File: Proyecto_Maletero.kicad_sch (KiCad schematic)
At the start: 1 part

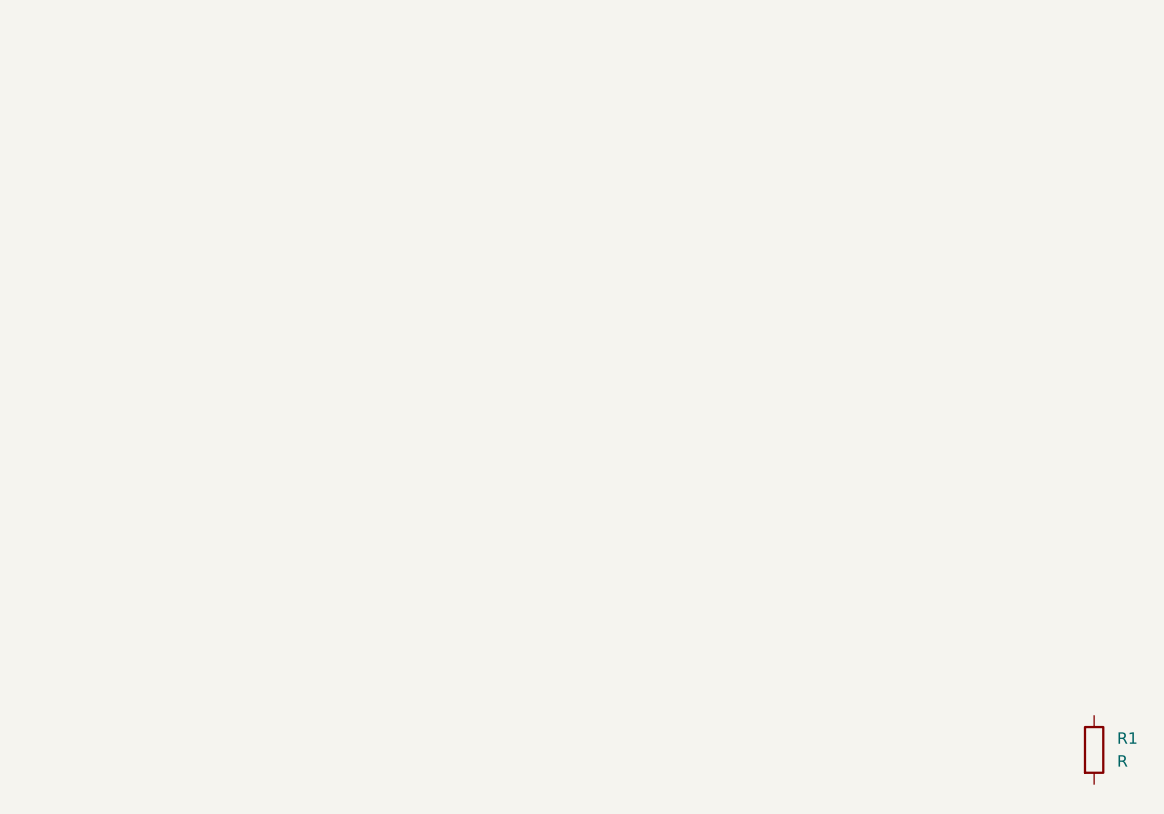
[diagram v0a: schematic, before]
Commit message: Adición conectores
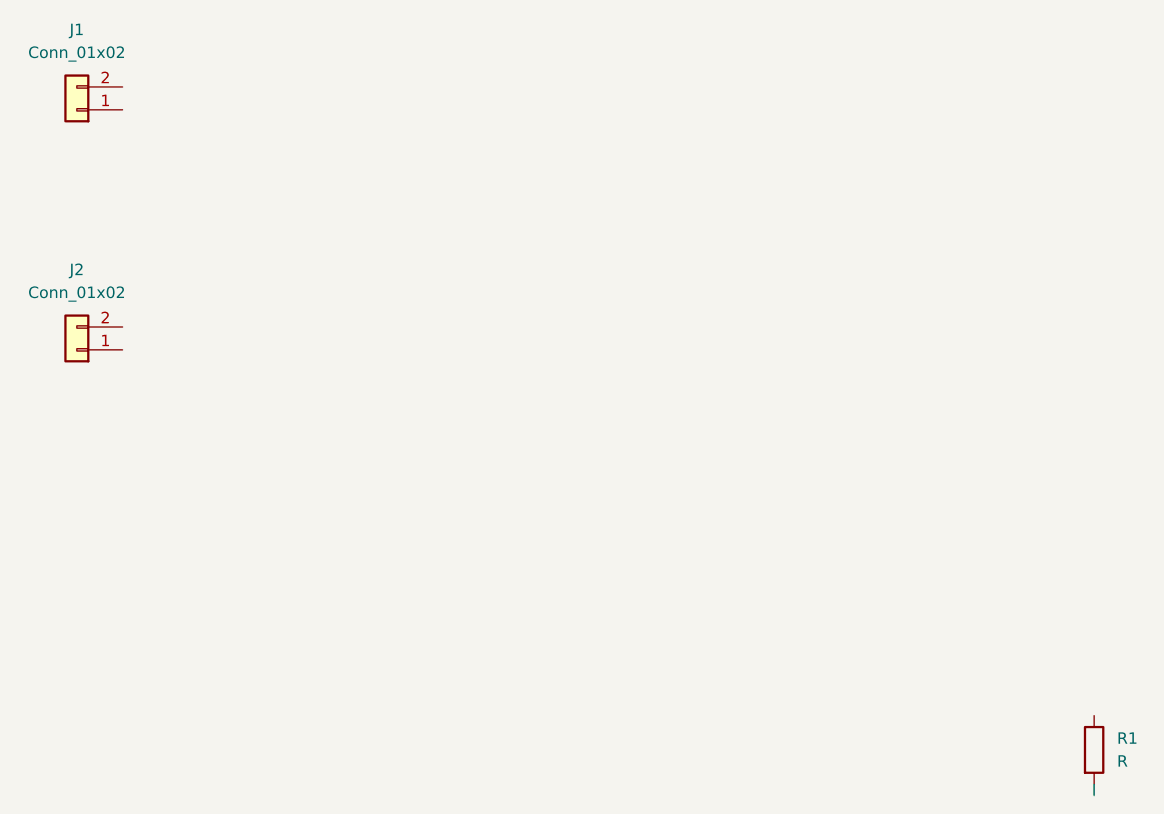
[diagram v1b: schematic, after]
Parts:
- added J1, J2: Conn_01x02, symbol Connector_Generic:Conn_01x02
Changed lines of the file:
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@@
 	(generator_version "9.0")
 	(paper "A4")
+	(wire
+		(pts
+			(xy 140.97 105.41) (xy 140.97 106.68)
+		)
+		(stroke
+			(width 0)
+			(type default)
+		)
+	)
+	(symbol
+		(lib_id "Connector_Generic:Conn_01x02")
+		(at 27.94 30.48 180)
+		(unit 1)
+		(exclude_from_sim no)
+		(in_bom yes)
+		(on_board yes)
+		(dnp no)
+		(fields_autoplaced yes)
+		(property "Reference" "J1"
+			(at 27.94 21.59 0)
+			(effects
+				(font
+					(size 1.27 1.27)
+				)
+			)
+		)
+		(property "Value" "Conn_01x02"
+			(at 27.94 24.13 0)
+			(effects
+				(font
+					(size 1.27 1.27)
+				)
+			)
+		)
+		(property "Footprint" ""
+			(at 27.94 30.48 0)
+			(effects
+				(font
+					(size 1.27 1.27)
+				)
+				(hide yes)
+			)
+		)
+		(property "Datasheet" "~"
+			(at 27.94 30.48 0)
+			(effects
+				(font
+					(size 1.27 1.27)
+				)
+				(hide yes)
+			)
+		)
+		(property "Description" "Generic connector, single row, 01x02, script generated (kicad-library-utils/schlib/autogen/connector/)"
+			(at 27.94 30.48 0)
+			(effects
+				(font
+					(size 1.27 1.27)
+				)
+				(hide yes)
+			)
+		)
+		(pin "2"
+		)
+		(pin "1"
+		)
+		(instances
+			(project ""
+				(path "/14c0d961-a62d-4b1a-b8ec-37f60ffee5fd"
+					(reference "J1")
+					(unit 1)
+				)
+			)
+		)
+	)
+	(symbol
+		(lib_id "Connector_Generic:Conn_01x02")
+		(at 27.94 57.15 180)
+		(unit 1)
+		(exclude_from_sim no)
+		(in_bom yes)
+		(on_board yes)
+		(dnp no)
+		(fields_autoplaced yes)
+		(property "Reference" "J2"
+			(at 27.94 48.26 0)
+			(effects
+				(font
+					(size 1.27 1.27)
+				)
+			)
+		)
+		(property "Value" "Conn_01x02"
+			(at 27.94 50.8 0)
+			(effects
+				(font
+					(size 1.27 1.27)
+				)
+			)
+		)
+		(property "Footprint" ""
+			(at 27.94 57.15 0)
+			(effects
+				(font
+					(size 1.27 1.27)
+				)
+				(hide yes)
+			)
+		)
+		(property "Datasheet" "~"
+			(at 27.94 57.15 0)
+			(effects
+				(font
+					(size 1.27 1.27)
+				)
+				(hide yes)
+			)
+		)
+		(property "Description" "Generic connector, single row, 01x02, script generated (kicad-library-utils/schlib/autogen/connector/)"
+			(at 27.94 57.15 0)
+			(effects
+				(font
+					(size 1.27 1.27)
+				)
+				(hide yes)
+			)
+		)
+		(pin "2"
+		)
+		(pin "1"
+		)
+		(instances
+			(project "Proyecto_Maletero"
+				(path "/14c0d961-a62d-4b1a-b8ec-37f60ffee5fd"
+					(reference "J2")
+					(unit 1)
+				)
+			)
+		)
+	)
 	(symbol
 		(lib_id "Device:R")

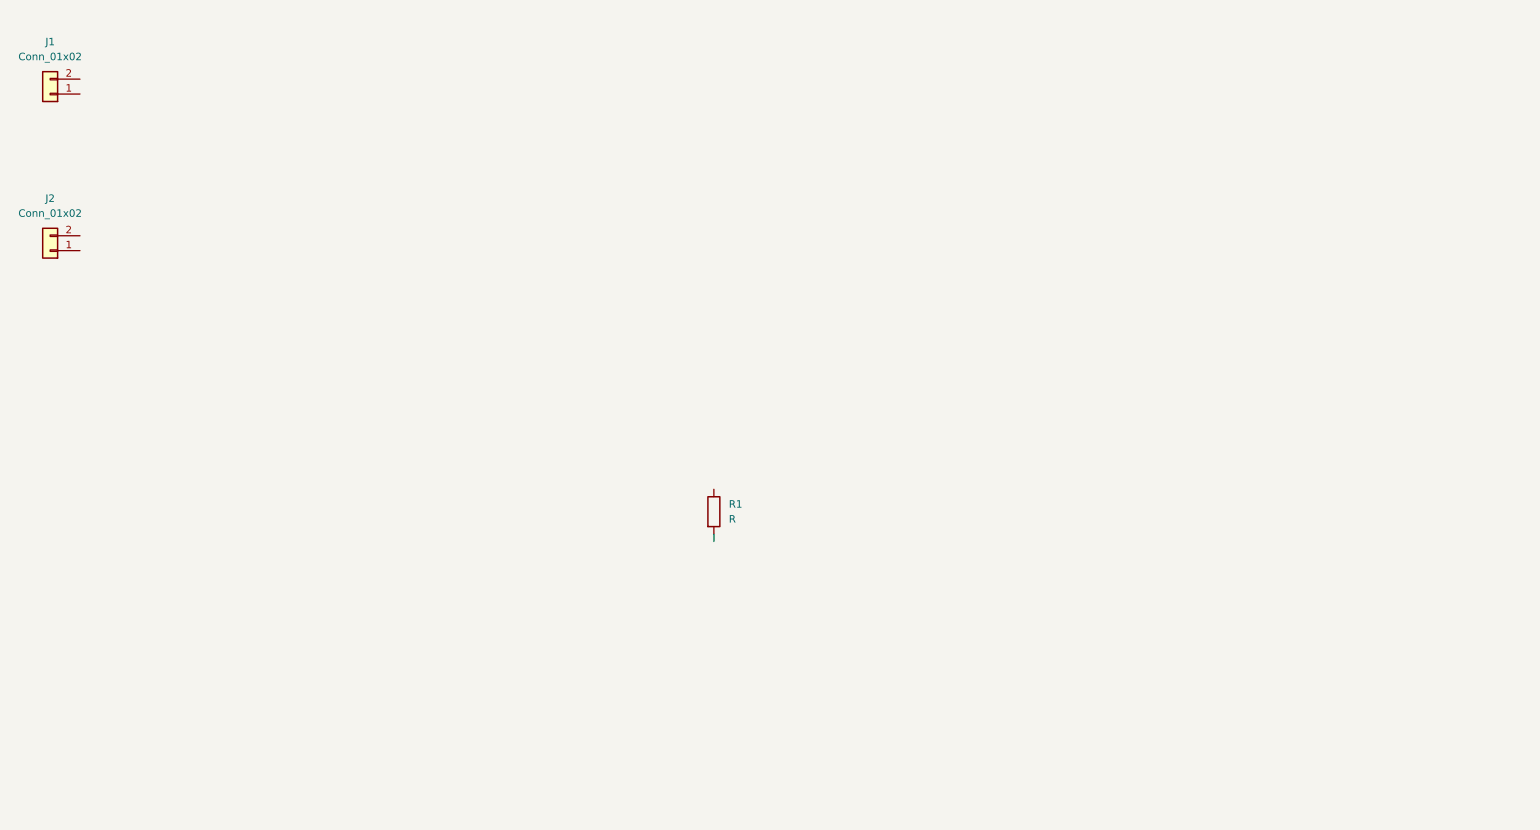
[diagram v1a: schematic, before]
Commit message: Etapa de regulacion (LT1117)
Hemos añadido una etapa de regulación  de VBAT.
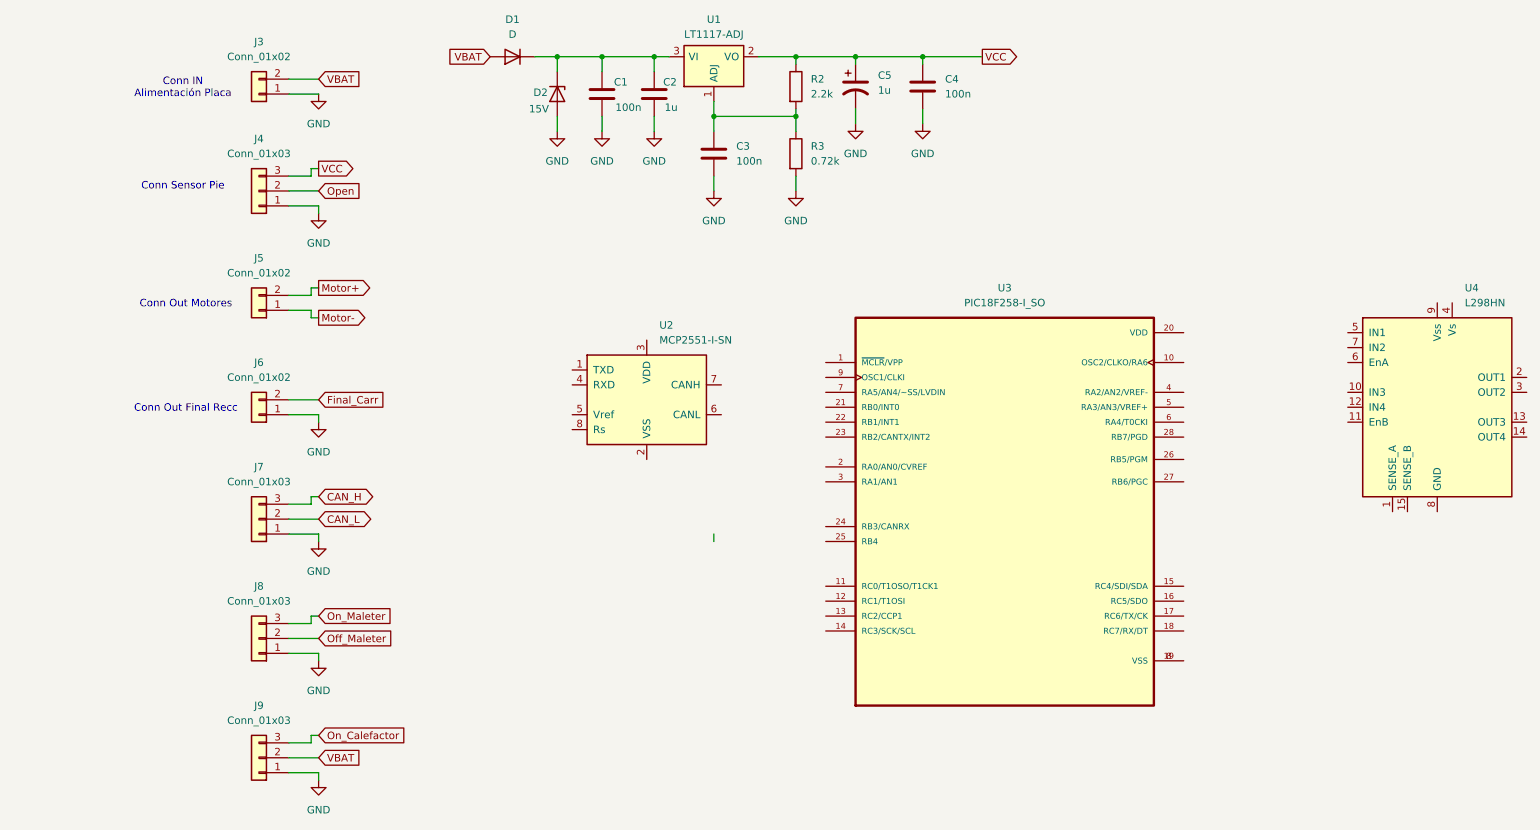
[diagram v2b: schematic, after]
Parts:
- removed J1, J2: Conn_01x02, symbol Connector_Generic:Conn_01x02
- removed R1: R, symbol Device:R
- added C1, C3, C4: 100n, symbol Device:C
- added C2: 1u, symbol Device:C
- added C5: 1u, symbol Device:C_Polarized_US
- added D1: D, symbol Device:D
- added D2: 15V, symbol Device:D_Zener
- added J3, J5, J6: Conn_01x02, TerminalBlock_Phoenix:TerminalBlock_Phoenix_MKDS-1,5-2-5.08_1x02_P5.08mm_Horizontal, symbol Connector_Generic:Conn_01x02
- added J4, J7, J8, J9: Conn_01x03, symbol Connector_Generic:Conn_01x03
- added R2: 2.2k, symbol Device:R
- added R3: 0.72k, symbol Device:R
- added U1: LT1117-ADJ, symbol Regulator_Linear:LT1117-ADJ
- added U2: MCP2551-I-SN, Package_SO:SOIC-8_3.9x4.9mm_P1.27mm, symbol Interface_CAN_LIN:MCP2551-I-SN
- added U3: PIC18F258-I_SO, PIC18F258-I_SO:SOIC127P1030X265-28N, symbol PIC18F258-I_SO:PIC18F258-I_SO
- added U4: L298HN, Package_TO_SOT_THT:TO-220-15_P2.54x2.54mm_StaggerOdd_Lead5.84mm_TabDown, symbol Driver_Motor:L298HN
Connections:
- new net: C3.1, R2.2, R3.1, U1.1 (ADJ)
- new net: C1.1, C2.1, D1.1 (K), D2.1 (K), U1.3 (VI)
- new net: U3.19 (VSS), U3.8 (VSS)
- new net CAN_H: J7.3 (Pin_3)
- new net CAN_L: J7.2 (Pin_2)
- new net Final_Carr: J6.2 (Pin_2)
- new net GND: C1.2, C2.2, C3.2, C4.2, C5.2, D2.2 (A), J3.1 (Pin_1), J4.1 (Pin_1), J6.1 (Pin_1), J7.1 (Pin_1), J8.1 (Pin_1), J9.1 (Pin_1), R3.2
- new net Motor+: J5.2 (Pin_2)
- new net Motor-: J5.1 (Pin_1)
- new net Off_Maleter: J8.2 (Pin_2)
- new net On_Calefactor: J9.3 (Pin_3)
- new net On_Maleter: J8.3 (Pin_3)
- new net Open: J4.2 (Pin_2)
- new net VBAT: D1.2 (A), J3.2 (Pin_2), J9.2 (Pin_2)
- new net VCC: C4.1, C5.1, J4.3 (Pin_3), R2.1, U1.2 (VO)
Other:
- note added: "Conn IN Alimentación Placa"
- note added: "Conn Out Final Recc"
- note added: "Conn Out Motores"
- note added: "Conn Sensor Pie"

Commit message: Compracion guardado
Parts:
- added U5: 4006, symbol 4xxx_IEEE:4006
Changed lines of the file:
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@@
+	)
+	(symbol
+		(lib_id "4xxx_IEEE:4006")
+		(at 115.57 114.3 0)
+		(unit 1)
+		(exclude_from_sim no)
+		(in_bom yes)
+		(on_board yes)
+		(dnp no)
+		(fields_autoplaced yes)
+		(property "Reference" "U5"
+			(at 117.7133 101.6 0)
+			(effects
+				(font
+					(size 1.27 1.27)
+				)
+				(justify left)
+			)
+		)
+		(property "Value" "4006"
+			(at 117.7133 104.14 0)
+			(effects
+				(font
+					(size 1.27 1.27)
+				)
+				(justify left)
+			)
+		)
+		(property "Footprint" ""
+			(at 115.57 114.3 0)
+			(effects
+				(font
+					(size 1.27 1.27)
+				)
+				(hide yes)
+			)
+		)
+		(property "Datasheet" ""
+			(at 115.57 114.3 0)
+			(effects
+				(font
+					(size 1.27 1.27)
+				)
+				(hide yes)
+			)
+		)
+		(property "Description" ""
+			(at 115.57 114.3 0)
+			(effects
+				(font
+					(size 1.27 1.27)
+				)
+				(hide yes)
+			)
+		)
+		(pin "6"
+		)
+		(pin "8"
+		)
+		(pin "14"
+		)
+		(pin "7"
+		)
+		(pin "3"
+		)
+		(pin "1"
+		)
+		(pin "4"
+		)
+		(pin "5"
+		)
+		(pin "13"
+		)
+		(pin "11"
+		)
+		(pin "12"
+		)
+		(pin "10"
+		)
+		(pin "9"
+		)
+		(instances
+			(project ""
+				(path "/14c0d961-a62d-4b1a-b8ec-37f60ffee5fd"
+					(reference "U5")
+					(unit 1)
+				)
+			)
+		)
 	)
 	(symbol

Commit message: Comprobación Guardado 2
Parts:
- removed U5: 4006, symbol 4xxx_IEEE:4006
- added C6: C, symbol Device:C
- added R4: 2.2k, symbol Device:R
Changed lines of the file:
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@@
-	(wire
-		(pts
-			(xy 140.97 105.41) (xy 140.97 106.68)
-		)
-		(stroke
-			(width 0)
-			(type default)
-		)
-	)
 	(wire
 		(pts
@@
 	)
 	(symbol
+		(lib_id "Device:C")
+		(at 118.11 110.49 0)
+		(unit 1)
+		(exclude_from_sim no)
+		(in_bom yes)
+		(on_board yes)
+		(dnp no)
+		(fields_autoplaced yes)
+		(property "Reference" "C6"
+			(at 121.92 109.2199 0)
+			(effects
+				(font
+					(size 1.27 1.27)
+				)
+				(justify left)
+			)
+		)
+		(property "Value" "C"
+			(at 121.92 111.7599 0)
+			(effects
+				(font
+					(size 1.27 1.27)
+				)
+				(justify left)
+			)
+		)
+		(property "Footprint" ""
+			(at 119.0752 114.3 0)
+			(effects
+				(font
+					(size 1.27 1.27)
+				)
+				(hide yes)
+			)
+		)
+		(property "Datasheet" "~"
+			(at 118.11 110.49 0)
+			(effects
+				(font
+					(size 1.27 1.27)
+				)
+				(hide yes)
+			)
+		)
+		(property "Description" "Unpolarized capacitor"
+			(at 118.11 110.49 0)
+			(effects
+				(font
+					(size 1.27 1.27)
+				)
+				(hide yes)
+			)
+		)
+		(pin "1"
+		)
+		(pin "2"
+		)
+		(instances
+			(project ""
+				(path "/14c0d961-a62d-4b1a-b8ec-37f60ffee5fd"
+					(reference "C6")
+					(unit 1)
+				)
+			)
+		)
+	)
+	(symbol
 		(lib_id "power:GND")
 		(at 154.94 46.99 0)
@@
 	)
 	(symbol
-		(lib_id "4xxx_IEEE:4006")
-		(at 115.57 114.3 0)
-		(unit 1)
-		(exclude_from_sim no)
-		(in_bom yes)
-		(on_board yes)
-		(dnp no)
-		(fields_autoplaced yes)
-		(property "Reference" "U5"
-			(at 117.7133 101.6 0)
-			(effects
-				(font
-					(size 1.27 1.27)
-				)
-				(justify left)
-			)
-		)
-		(property "Value" "4006"
-			(at 117.7133 104.14 0)
+		(lib_id "Device:R")
+		(at 132.08 111.76 0)
+		(unit 1)
+		(exclude_from_sim no)
+		(in_bom yes)
+		(on_board yes)
+		(dnp no)
+		(fields_autoplaced yes)
+		(property "Reference" "R4"
+			(at 134.62 110.4899 0)
+			(effects
+				(font
+					(size 1.27 1.27)
+				)
+				(justify left)
+			)
+		)
+		(property "Value" "2.2k"
+			(at 134.62 113.0299 0)
 			(effects
 				(font
@@
 		)
 		(property "Footprint" ""
-			(at 115.57 114.3 0)
-			(effects
-				(font
-					(size 1.27 1.27)
-				)
-				(hide yes)
-			)
-		)
-		(property "Datasheet" ""
-			(at 115.57 114.3 0)
-			(effects
-				(font
-					(size 1.27 1.27)
-				)
-				(hide yes)
-			)
-		)
-		(property "Description" ""
-			(at 115.57 114.3 0)
-			(effects
-				(font
-					(size 1.27 1.27)
-				)
-				(hide yes)
-			)
-		)
-		(pin "6"
-		)
-		(pin "8"
-		)
-		(pin "14"
-		)
-		(pin "7"
-		)
-		(pin "3"
-		)
-		(pin "1"
-		)
-		(pin "4"
-		)
-		(pin "5"
-		)
-		(pin "13"
-		)
-		(pin "11"
-		)
-		(pin "12"
-		)
-		(pin "10"
-		)
-		(pin "9"
-		)
-		(instances
-			(project ""
-				(path "/14c0d961-a62d-4b1a-b8ec-37f60ffee5fd"
-					(reference "U5")
-					(unit 1)
-				)
+			(at 130.302 111.76 90)
+			(effects
+				(font
+					(size 1.27 1.27)
+				)
+				(hide yes)
+			)
+		)
+		(property "Datasheet" "~"
+			(at 132.08 111.76 0)
+			(effects
+				(font
+					(size 1.27 1.27)
+				)
+				(hide yes)
+			)
+		)
+		(property "Description" "Resistor"
+			(at 132.08 111.76 0)
+			(effects
+				(font
+					(size 1.27 1.27)
+				)
+				(hide yes)
+			)
+		)
+		(pin "2"
+		)
+		(pin "1"
+		)
+		(instances
+			(project "Proyecto_Maletero"
+				(path "/14c0d961-a62d-4b1a-b8ec-37f60ffee5fd"
+					(reference "R4")
+					(unit 1)
+				)
